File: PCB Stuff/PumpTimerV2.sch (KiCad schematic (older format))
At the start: 31 parts, among them J1 1935161, J2 282856-2, J3 282856-2, J4 Conn_02x20_Odd_Even, J6 B4B-PH-SM4-TBT(LF)(SN), K1 ADW1205HLW, K2 ADW1205HLW, Q1 DMN67D7L, Q2 DMN67D7L, SW1 TL3305AF160QG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

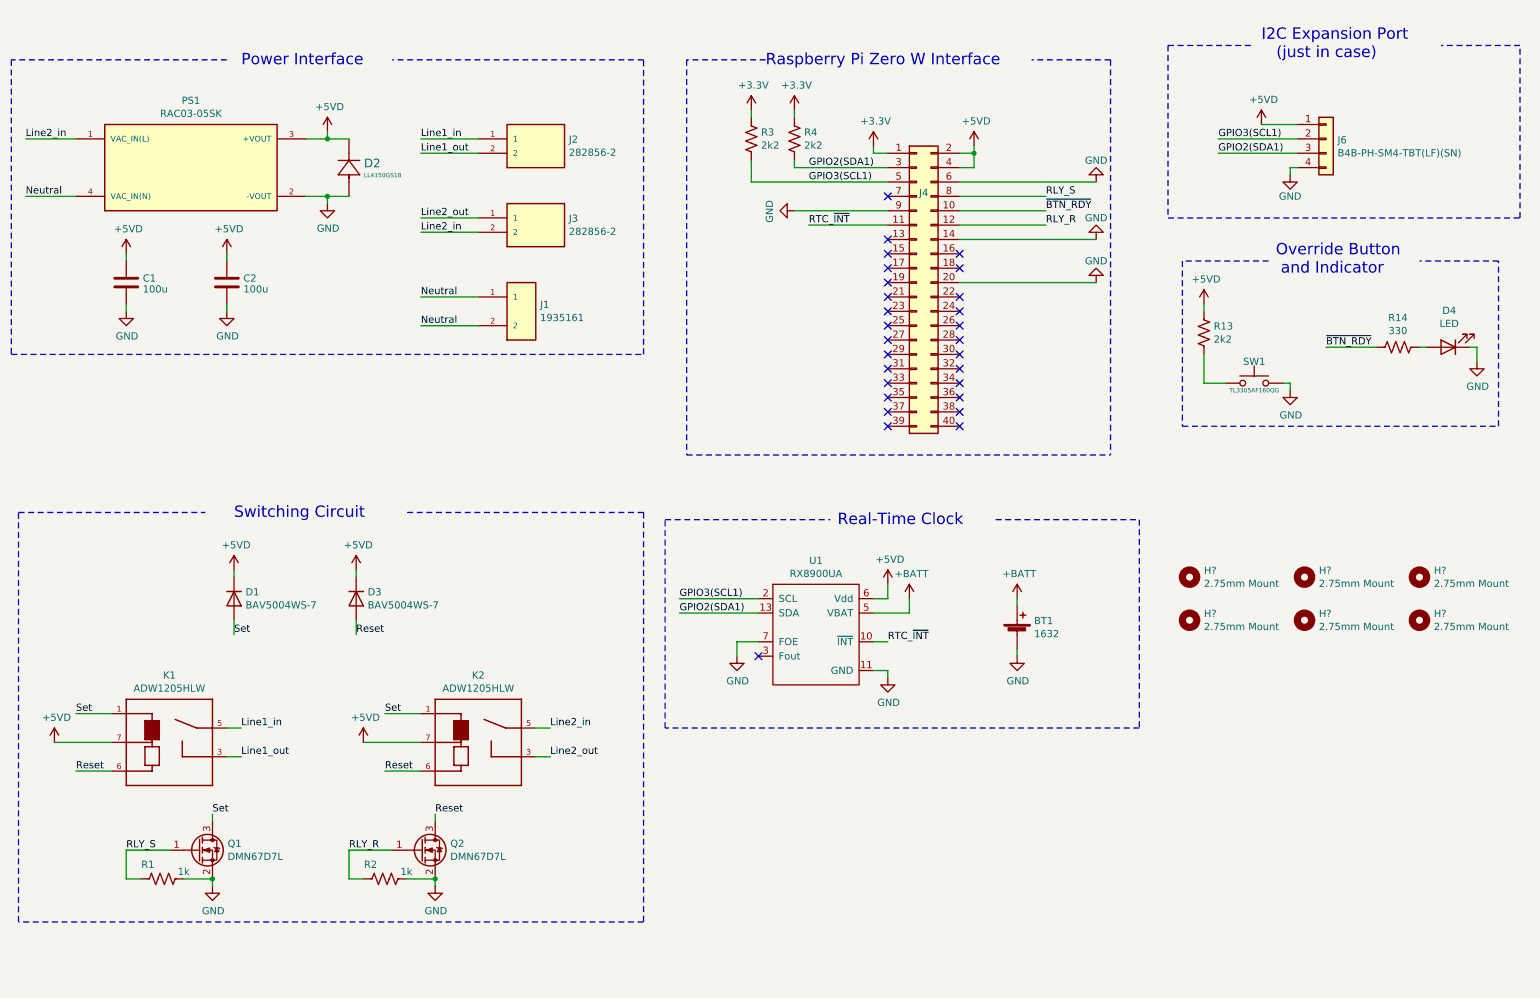
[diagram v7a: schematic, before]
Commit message: Making sure schematic and PCB match. Finished re-routing after flipping rpi header.
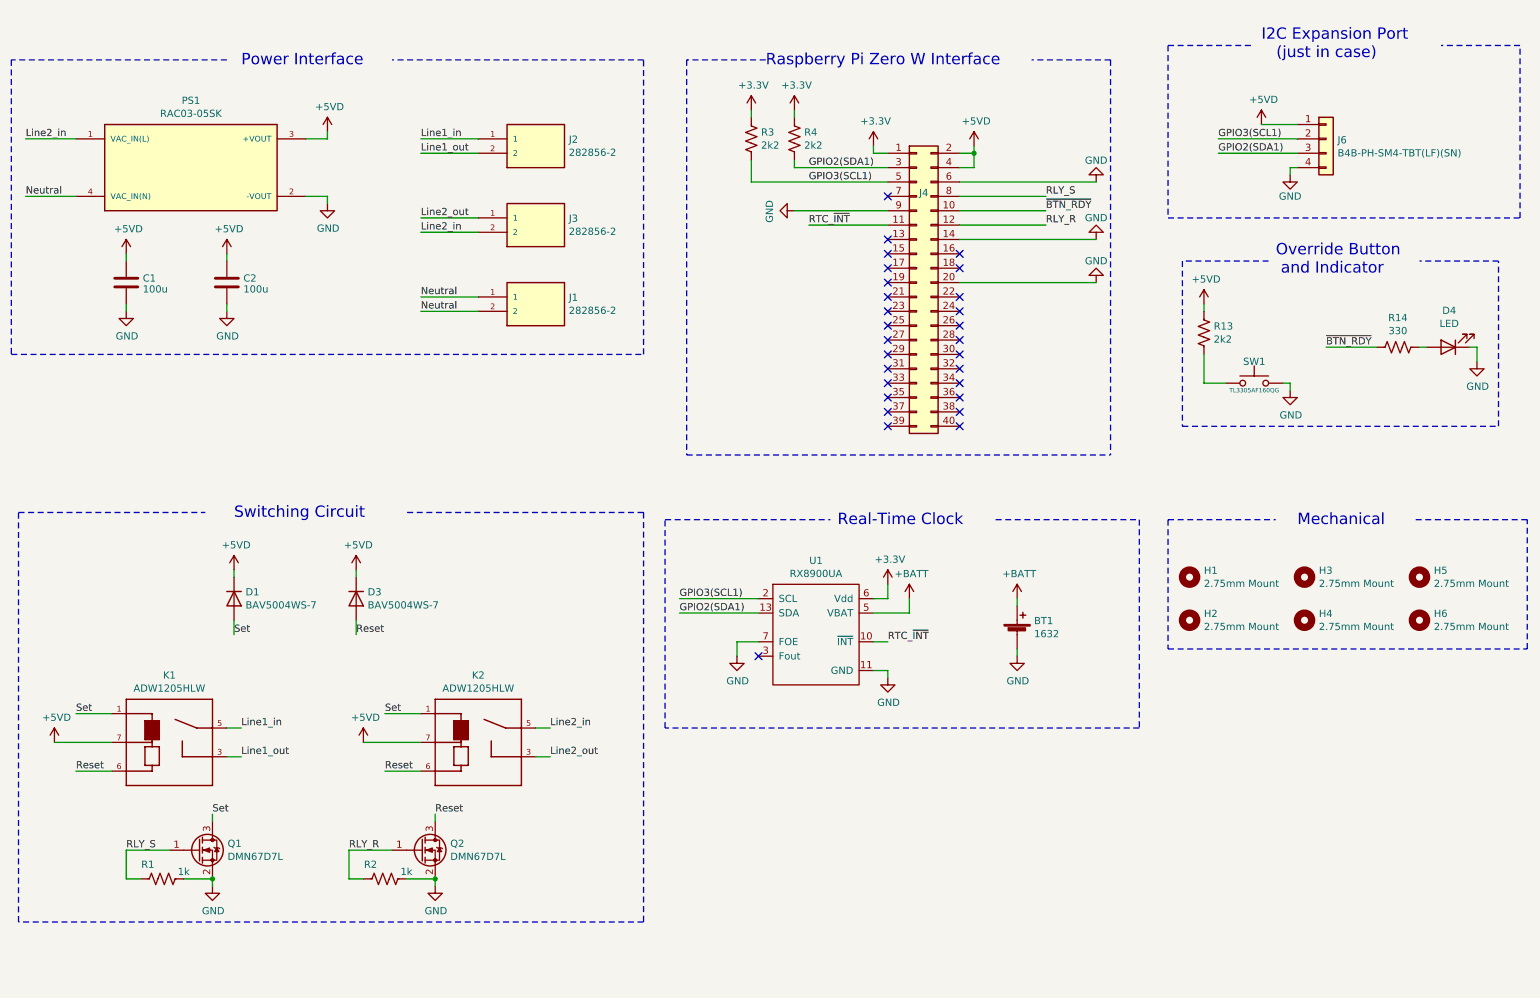
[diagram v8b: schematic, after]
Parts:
- removed D2: LL4150GS18, Diode_SMD:D_SOD-80, symbol Diode:Generic_Diode
- removed J1: 1935161, PHOENIX_1935161, symbol Connector:1935161
- added J1: 282856-2, TE_282856-2, symbol Connector:282856-2
- gave numbers to parts that had none: 6
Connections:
- net +3V3: now also U1.6 (Vdd)
- net +5VD: no longer U1.6 (Vdd)
- net Neutral: now also J1.1, J1.2
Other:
- note added: "Mechanical"
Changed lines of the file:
@@
-$EndComp
-$Comp
-L Diode:Generic_Diode D2
-U 1 1 607648B8
-P 2950 2150
-F 0 "D2" V 3180 2046 60  0000 R CNN
-F 1 "LL4150GS18" V 3097 2046 30  0000 R CNN
-F 2 "Diode_SMD:D_SOD-80" H 3150 1790 60  0001 C CNN
-F 3 "" H 2950 2150 60  0000 C CNN
-	1    2950 2150
-	0    -1   -1   0
 $EndComp
 $Comp
@@
 	1    0    0    -1
 $EndComp
-Wire Wire Line
-	2950 1750 2800 1750
-Connection ~ 2800 1750
-Wire Wire Line
-	2950 2150 2800 2150
-Connection ~ 2800 2150
 $Comp
 L power:+5VD #PWR01
@@
 $EndComp
 $Comp
-L power:+5VD #PWR019
+L power:+3.3V #PWR019
 U 1 1 6077EE23
 P 6700 4850
 F 0 "#PWR019" H 6700 4700 50  0001 C CNN
-F 1 "+5VD" H 6715 5023 50  0000 C CNN
+F 1 "+3.3V" H 6715 5023 50  0000 C CNN
 F 2 "" H 6700 4850 50  0001 C CNN
 F 3 "" H 6700 4850 50  0001 C CNN
@@
 	8250 1200 7700 1200
 Wire Wire Line
-	3850 3050 3450 3050
+	3850 2950 3450 2950
 Wire Wire Line
 	3450 2850 3850 2850
@@
 Wire Wire Line
 	3450 2300 3850 2300
-Text Label 3450 3050 0    50   ~ 0
+Text Label 3450 2950 0    50   ~ 0
 Neutral
 Text Label 3450 2850 0    50   ~ 0
@@
 Text Label 3450 1750 0    50   ~ 0
 Line1_in
-$Comp
-L Connector:1935161 J1
-U 1 1 6075587C
-P 4150 2950
-F 0 "J1" H 4280 2996 50  0000 L CNN
-F 1 "1935161" H 4280 2905 50  0000 L CNN
-F 2 "PHOENIX_1935161" H 4150 2950 50  0001 L BNN
-F 3 "" H 4150 2950 50  0001 L BNN
-F 4 "Phoenix Contact" H 4150 2950 50  0001 L BNN "MANUFACTURER"
-	1    4150 2950
-	1    0    0    -1
-$EndComp
 $Comp
 L Connector:282856-2 J3
@@
 NoConn ~ 6700 2650
 $Comp
-L Mechanical:MountingHole H?
+L Mechanical:MountingHole H1
 U 1 1 608325BA
 P 8800 4800
-F 0 "H?" H 8900 4846 50  0000 L CNN
+F 0 "H1" H 8900 4846 50  0000 L CNN
 F 1 "2.75mm Mount" H 8900 4755 50  0000 L CNN
 F 2 "MountingHole:MountingHole_2.7mm_M2.5" H 8800 4800 50  0001 C CNN
@@
 $EndComp
 $Comp
-L Mechanical:MountingHole H?
+L Mechanical:MountingHole H3
 U 1 1 6083A38E
 P 9600 4800
-F 0 "H?" H 9700 4846 50  0000 L CNN
+F 0 "H3" H 9700 4846 50  0000 L CNN
 F 1 "2.75mm Mount" H 9700 4755 50  0000 L CNN
 F 2 "MountingHole:MountingHole_2.7mm_M2.5" H 9600 4800 50  0001 C CNN
@@
 $EndComp
 $Comp
-L Mechanical:MountingHole H?
+L Mechanical:MountingHole H5
 U 1 1 6083AA2B
 P 10400 4800
-F 0 "H?" H 10500 4846 50  0000 L CNN
+F 0 "H5" H 10500 4846 50  0000 L CNN
 F 1 "2.75mm Mount" H 10500 4755 50  0000 L CNN
 F 2 "MountingHole:MountingHole_2.7mm_M2.5" H 10400 4800 50  0001 C CNN
@@
 $EndComp
 $Comp
-L Mechanical:MountingHole H?
+L Mechanical:MountingHole H6
 U 1 1 608414EE
 P 10400 5100
-F 0 "H?" H 10500 5146 50  0000 L CNN
+F 0 "H6" H 10500 5146 50  0000 L CNN
 F 1 "2.75mm Mount" H 10500 5055 50  0000 L CNN
 F 2 "MountingHole:MountingHole_2.7mm_M2.5" H 10400 5100 50  0001 C CNN
@@
 $EndComp
 $Comp
-L Mechanical:MountingHole H?
+L Mechanical:MountingHole H4
 U 1 1 60841853
 P 9600 5100
-F 0 "H?" H 9700 5146 50  0000 L CNN
+F 0 "H4" H 9700 5146 50  0000 L CNN
 F 1 "2.75mm Mount" H 9700 5055 50  0000 L CNN
 F 2 "MountingHole:MountingHole_2.7mm_M2.5" H 9600 5100 50  0001 C CNN
@@
 $EndComp
 $Comp
-L Mechanical:MountingHole H?
+L Mechanical:MountingHole H2
 U 1 1 60841D9C
 P 8800 5100
-F 0 "H?" H 8900 5146 50  0000 L CNN
+F 0 "H2" H 8900 5146 50  0000 L CNN
 F 1 "2.75mm Mount" H 8900 5055 50  0000 L CNN
 F 2 "MountingHole:MountingHole_2.7mm_M2.5" H 8800 5100 50  0001 C CNN
@@
 	1    0    0    -1
 $EndComp
+$Comp
+L Connector:282856-2 J1
+U 1 1 6083B1AC
+P 4250 2950
+F 0 "J1" H 4480 3046 50  0000 L CNN
+F 1 "282856-2" H 4480 2955 50  0000 L CNN
+F 2 "TE_282856-2" H 4250 2950 50  0001 L BNN
+F 3 "" H 4250 2950 50  0001 L BNN
+F 4 "Compliant with Exemptions" H 4250 2950 50  0001 L BNN "EU_RoHS_Compliance"
+F 5 "282856-2" H 4250 2950 50  0001 L BNN "Comment"
+	1    4250 2950
+	1    0    0    -1
+$EndComp
+Wire Notes Line width 10 style solid
+	8650 4400 8650 5300
+Wire Notes Line width 10 style solid
+	8650 5300 11150 5300
+Wire Notes Line width 10 style solid
+	11150 5300 11150 4400
+Wire Notes Line width 10 style solid
+	11150 4400 10350 4400
+Wire Notes Line width 10 style solid
+	8650 4400 9400 4400
+Text Notes 9550 4450 0    79   ~ 0
+Mechanical
 $EndSCHEMATC
